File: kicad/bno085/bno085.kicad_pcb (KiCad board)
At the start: 2 copper layers, 31 x 42 mm, 41 parts, among them J1 USB4125-GF-A_REVA, J2 PinHeader_2x03_P2.54mm_Vertic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, J3 PinHeader_1x05_P2.54mm_Vertic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, J4 PinHeader_1x02_P2.54mm_Vertic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, SW1 SW_SPDT, U1 dfn-8_wide, U2 BQ297xy, U3 CSD85302L, U4 NCP177BMX330TCG, U5 ASAK-32.7680KHZ-LRS-T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

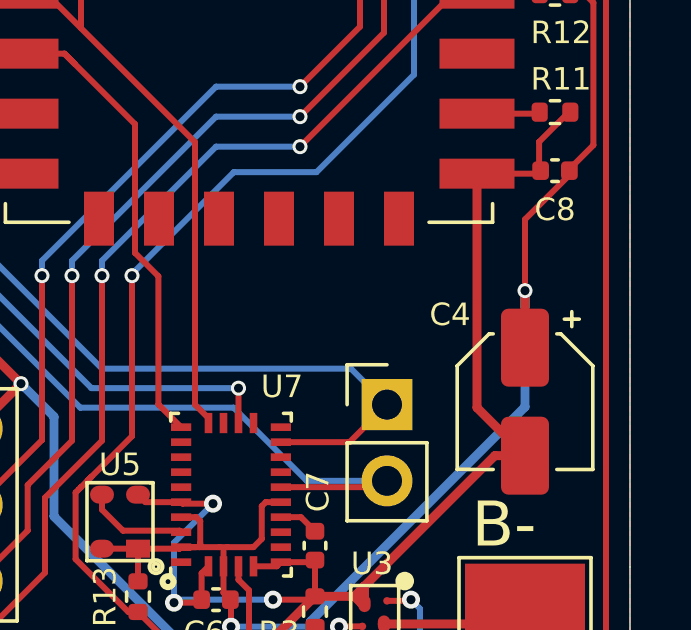
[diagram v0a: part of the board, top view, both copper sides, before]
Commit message: made minor cahnges to bno085 schimatic + pcb to better reflect the real world version
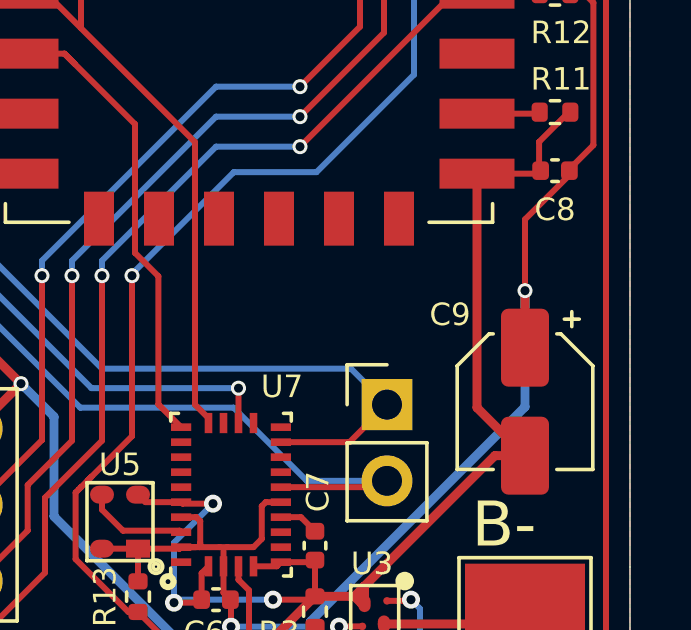
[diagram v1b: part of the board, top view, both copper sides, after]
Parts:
- renumbered C4 to C9
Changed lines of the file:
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@@
     (tags "capacitor electrolytic")
     (attr smd)
-    (fp_text reference "C4" (at -2.9 2.5 180) (layer "F.SilkS")
+    (fp_text reference "C9" (at -2.9 2.5 180) (layer "F.SilkS")
       (effects (font (size 0.75 0.75) (thickness 0.15)))
     )
@@
     (property "Sheetname" "")
     (attr smd)
-    (fp_text reference "C4" (at 2.2 0.1 180) (layer "F.SilkS")
-      (effects (font (size 0.75 0.75) (thickness 0.15)))
-    )
+    (fp_text reference "C4" (at 2.2 0.1) (layer "F.SilkS")
+      (effects (font (size 0.75 0.75) (thickness 0.15)))
+    )
